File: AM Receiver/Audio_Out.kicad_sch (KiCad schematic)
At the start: 15 parts, among them P101 50k 10% Trimmer, Q102 BC547, Q103 BC547, Q104 BC557

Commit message: Filled out information in User.Drawings on PCB
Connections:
- net +12V ...+15V renamed VIN
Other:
- note added: "Design Notes - Audio Out Audio_Out ist das demodulierte NF-Signal aus dem AM/ZF-Teil. P101 = 50k stellt Pegel/Verstärkung der Treiberstufe ein. C129 = 100 nF ist die Eingangskopplung; Grenzfrequenz mit Quell-/Poti-R: fc = 1/(2*pi*R*C). Q102/Q103/Q104 bilden eine diskrete Class-AB Ausgangsstufe. D100/D101 erzeugen die Bias-Spannung zur Reduktion der Übernahmeverzerrung. C132 = 470 uF koppelt den L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"
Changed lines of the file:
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@@
 		(comment 3 "T. Brown")
+	)
+	(text "Design Notes - Audio Out\nAudio_Out ist das demodulierte NF-Signal aus dem AM/ZF-Teil.\nP101 = 50k stellt Pegel/Verstärkung der Treiberstufe ein.\nC129 = 100 nF ist die Eingangskopplung; Grenzfrequenz mit Quell-/Poti-R: fc = 1/(2*pi*R*C).\nQ102/Q103/Q104 bilden eine diskrete Class-AB Ausgangsstufe.\nD100/D101 erzeugen die Bias-Spannung zur Reduktion der Übernahmeverzerrung.\nC132 = 470 uF koppelt den Lautsprecher aus: fc ca. 42 Hz bei 8 Ohm, ca. 11 Hz bei 32 Ohm.\nR115 = 100R begrenzt den Ausgangs-/Basisstrom und verbessert die Stabilitaet."
+		(exclude_from_sim no)
+		(at 35.56 34.29 0)
+		(effects
+			(font
+				(size 1.27 1.27)
+			)
+			(justify left)
+		)
 	)
 	(junction
@@
 			)
 		)
-		(property "Value" "+12V ...+15V"
+		(property "Value" "VIN"
 			(at 143.51 50.8 0)
 			(show_name no)

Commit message: Updated Design notes in schematic
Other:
- note added: "Design Notes - Audio Out Audio_Out ist das demodulierte NF-Signal aus dem AM/ZF-Teil. P101 = 50k stellt Pegel/Verstaerkung der Treiberstufe ein. C129 = 100 nF ist die Eingangskopplung; Grenzfrequenz mit Quell-/Poti-R: fc = 1/(2*pi*R*C). Q102 arbeitet als Treiber; Q103/Q104 bilden die komplementaere Class-AB Ausgangsstufe. D100/D101 erzeugen die Bias-Spannung zur Reduktion der Uebernahmeverzerrung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"
- note removed: "Design Notes - Audio Out Audio_Out ist das demodulierte NF-Signal aus dem AM/ZF-Teil. P101 = 50k stellt Pegel/Verstärkung der Treiberstufe ein. C129 = 100 nF ist die Eingangskopplung; Grenzfrequenz mit Quell-/Poti-R: fc = 1/(2*pi*R*C). Q102/Q103/Q104 bilden eine diskrete Class-AB Ausgangsstufe. D100/D101 erzeugen die Bias-Spannung zur Reduktion der Übernahmeverzerrung. C132 = 470 uF koppelt den L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"
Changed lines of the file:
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@@
 		(comment 3 "T. Brown")
 	)
-	(text "Design Notes - Audio Out\nAudio_Out ist das demodulierte NF-Signal aus dem AM/ZF-Teil.\nP101 = 50k stellt Pegel/Verstärkung der Treiberstufe ein.\nC129 = 100 nF ist die Eingangskopplung; Grenzfrequenz mit Quell-/Poti-R: fc = 1/(2*pi*R*C).\nQ102/Q103/Q104 bilden eine diskrete Class-AB Ausgangsstufe.\nD100/D101 erzeugen die Bias-Spannung zur Reduktion der Übernahmeverzerrung.\nC132 = 470 uF koppelt den Lautsprecher aus: fc ca. 42 Hz bei 8 Ohm, ca. 11 Hz bei 32 Ohm.\nR115 = 100R begrenzt den Ausgangs-/Basisstrom und verbessert die Stabilitaet."
+	(text "Design Notes - Audio Out\nAudio_Out ist das demodulierte NF-Signal aus dem AM/ZF-Teil.\nP101 = 50k stellt Pegel/Verstaerkung der Treiberstufe ein.\nC129 = 100 nF ist die Eingangskopplung; Grenzfrequenz mit Quell-/Poti-R: fc = 1/(2*pi*R*C).\nQ102 arbeitet als Treiber; Q103/Q104 bilden die komplementaere Class-AB Ausgangsstufe.\nD100/D101 erzeugen die Bias-Spannung zur Reduktion der Uebernahmeverzerrung.\nC132 = 470 uF koppelt den Lautsprecher aus: fc ca. 42 Hz bei 8 Ohm, ca. 11 Hz bei 32 Ohm.\nR115 = 100R liegt im Treiber-/Emitterpfad und begrenzt Strom bzw. verbessert die Stabilitaet."
 		(exclude_from_sim no)
 		(at 35.56 34.29 0)

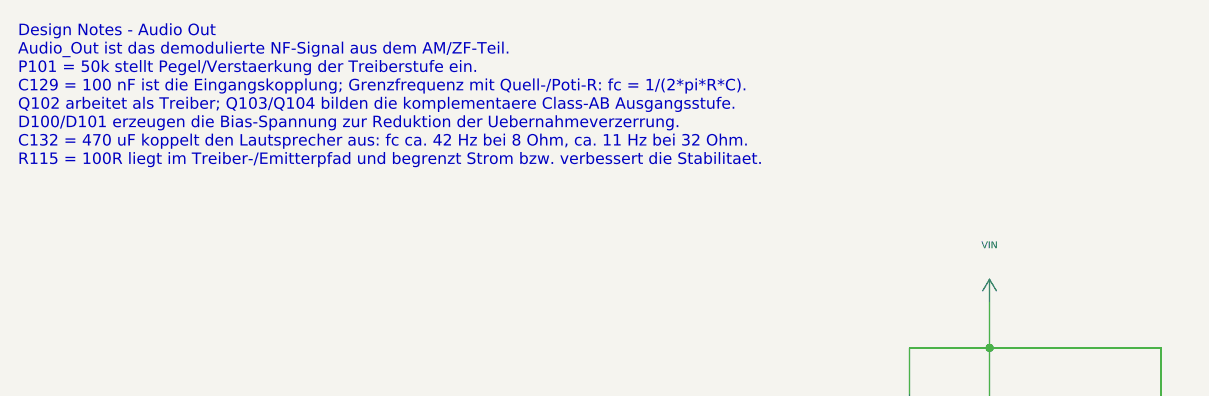
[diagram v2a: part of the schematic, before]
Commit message: updated schematic root page voltage
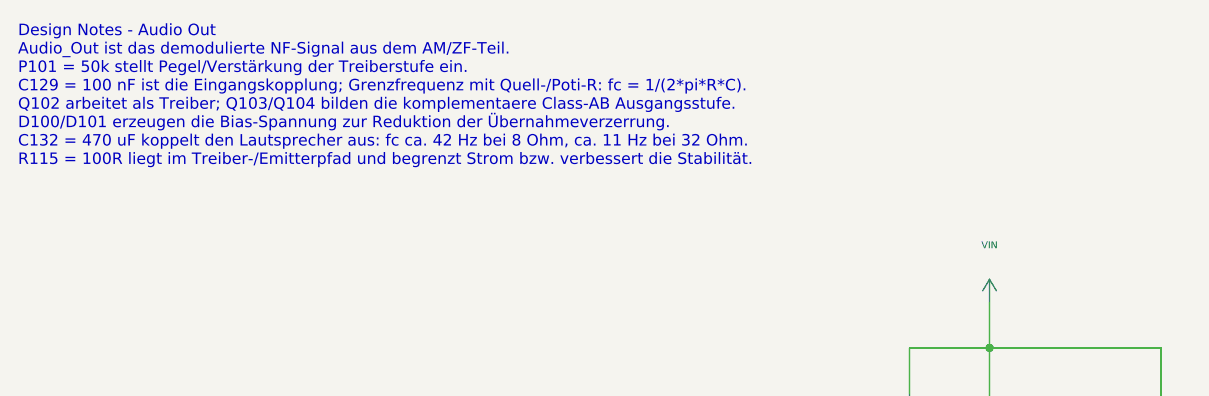
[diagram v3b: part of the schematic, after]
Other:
- note added: "Design Notes - Audio Out Audio_Out ist das demodulierte NF-Signal aus dem AM/ZF-Teil. P101 = 50k stellt Pegel/Verstärkung der Treiberstufe ein. C129 = 100 nF ist die Eingangskopplung; Grenzfrequenz mit Quell-/Poti-R: fc = 1/(2*pi*R*C). Q102 arbeitet als Treiber; Q103/Q104 bilden die komplementaere Class-AB Ausgangsstufe. D100/D101 erzeugen die Bias-Spannung zur Reduktion der Übernahmeverzerrung. 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"
- note removed: "Design Notes - Audio Out Audio_Out ist das demodulierte NF-Signal aus dem AM/ZF-Teil. P101 = 50k stellt Pegel/Verstaerkung der Treiberstufe ein. C129 = 100 nF ist die Eingangskopplung; Grenzfrequenz mit Quell-/Poti-R: fc = 1/(2*pi*R*C). Q102 arbeitet als Treiber; Q103/Q104 bilden die komplementaere Class-AB Ausgangsstufe. D100/D101 erzeugen die Bias-Spannung zur Reduktion der Uebernahmeverzerrung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"
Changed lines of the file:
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@@
 		(comment 3 "T. Brown")
 	)
-	(text "Design Notes - Audio Out\nAudio_Out ist das demodulierte NF-Signal aus dem AM/ZF-Teil.\nP101 = 50k stellt Pegel/Verstaerkung der Treiberstufe ein.\nC129 = 100 nF ist die Eingangskopplung; Grenzfrequenz mit Quell-/Poti-R: fc = 1/(2*pi*R*C).\nQ102 arbeitet als Treiber; Q103/Q104 bilden die komplementaere Class-AB Ausgangsstufe.\nD100/D101 erzeugen die Bias-Spannung zur Reduktion der Uebernahmeverzerrung.\nC132 = 470 uF koppelt den Lautsprecher aus: fc ca. 42 Hz bei 8 Ohm, ca. 11 Hz bei 32 Ohm.\nR115 = 100R liegt im Treiber-/Emitterpfad und begrenzt Strom bzw. verbessert die Stabilitaet."
+	(text "Design Notes - Audio Out\nAudio_Out ist das demodulierte NF-Signal aus dem AM/ZF-Teil.\nP101 = 50k stellt Pegel/Verstärkung der Treiberstufe ein.\nC129 = 100 nF ist die Eingangskopplung; Grenzfrequenz mit Quell-/Poti-R: fc = 1/(2*pi*R*C).\nQ102 arbeitet als Treiber; Q103/Q104 bilden die komplementaere Class-AB Ausgangsstufe.\nD100/D101 erzeugen die Bias-Spannung zur Reduktion der Übernahmeverzerrung.\nC132 = 470 uF koppelt den Lautsprecher aus: fc ca. 42 Hz bei 8 Ohm, ca. 11 Hz bei 32 Ohm.\nR115 = 100R liegt im Treiber-/Emitterpfad und begrenzt Strom bzw. verbessert die Stabilität."
 		(exclude_from_sim no)
 		(at 35.56 34.29 0)
